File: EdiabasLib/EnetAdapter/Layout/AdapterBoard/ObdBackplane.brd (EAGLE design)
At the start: 32 x 19.5 mm, 10 parts

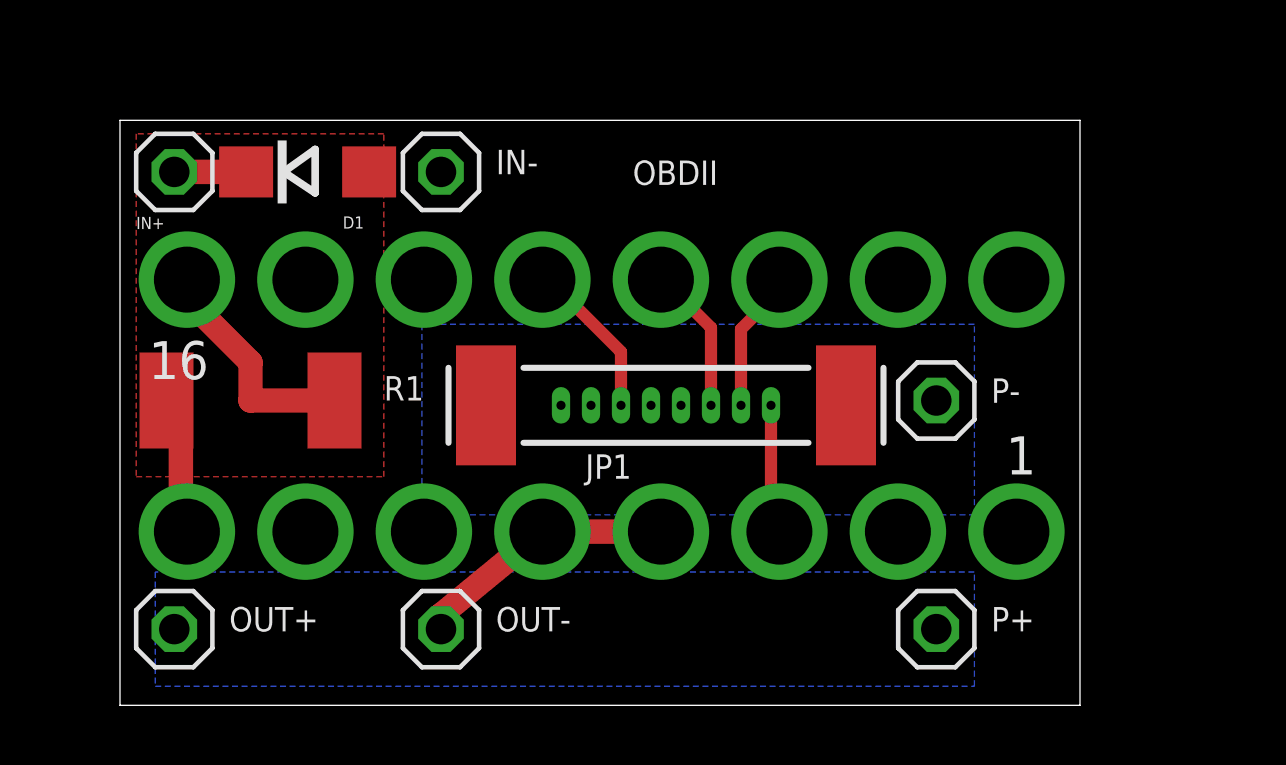
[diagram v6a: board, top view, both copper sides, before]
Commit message: Connector moved
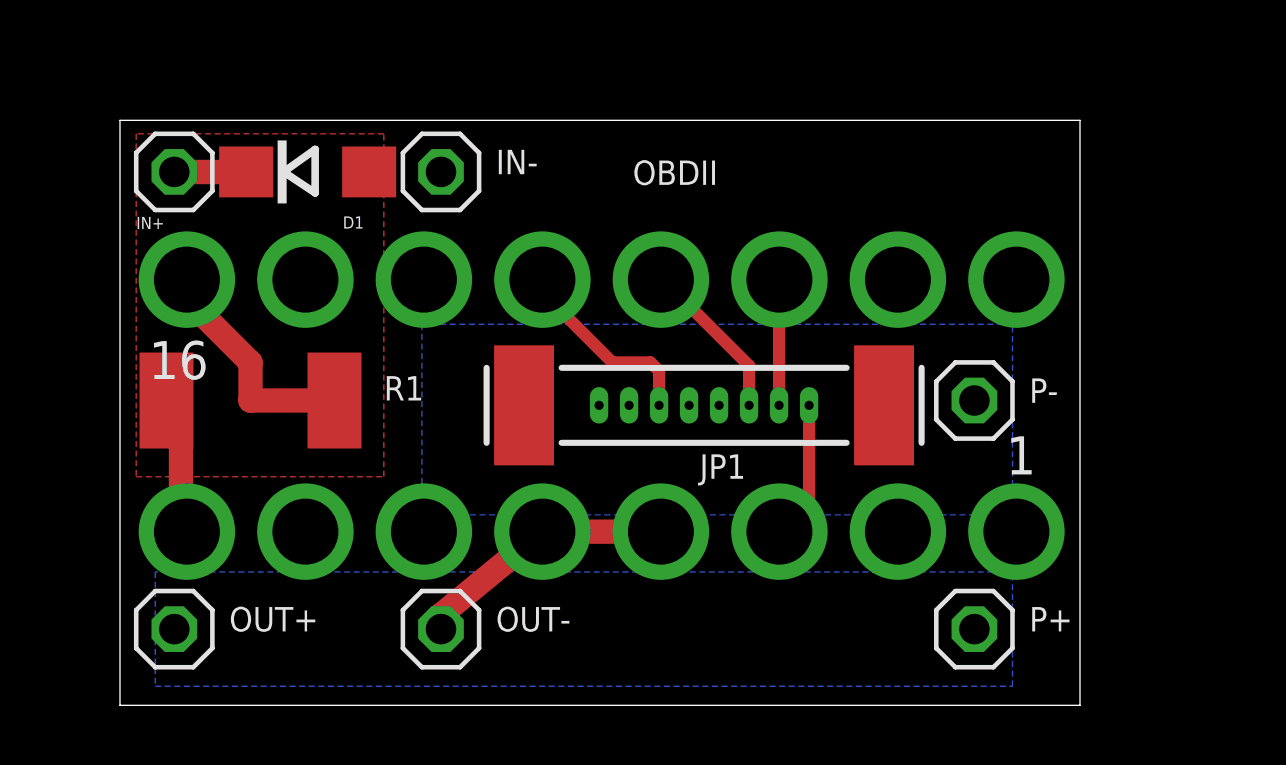
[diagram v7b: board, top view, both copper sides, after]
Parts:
- moved JP1 1.27 mm to (21.5, 10.0)
- moved P+ 1.27 mm to (30.5, 2.54)
- moved P- 1.27 mm to (30.5, 10.2)
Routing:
- net N$6: track 5.40 -> 6.55 mm
- net N$4: track 4.92 -> 5.45 mm
- net N$7: track 4.72 -> 4.19 mm
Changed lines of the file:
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@@
 <attribute name="VALUE" x="10.795" y="8.89" size="0.8128" layer="27"/>
 </element>
-<element name="P+" library="pinhead" package="1X01" value="5V" x="29.21" y="2.54" smashed="yes">
-<attribute name="NAME" x="31.0388" y="2.4638" size="0.8128" layer="25" ratio="10"/>
-<attribute name="VALUE" x="31.115" y="1.27" size="0.8128" layer="27"/>
+<element name="P+" library="pinhead" package="1X01" value="5V" x="30.48" y="2.54" smashed="yes">
+<attribute name="NAME" x="32.3088" y="2.4638" size="0.8128" layer="25" ratio="10"/>
+<attribute name="VALUE" x="32.385" y="1.27" size="0.8128" layer="27"/>
 </element>
-<element name="P-" library="pinhead" package="1X01" value="GND" x="29.21" y="10.16" smashed="yes">
-<attribute name="NAME" x="31.0388" y="10.0838" size="0.8128" layer="25" ratio="10"/>
-<attribute name="VALUE" x="30.48" y="8.89" size="0.8128" layer="27"/>
+<element name="P-" library="pinhead" package="1X01" value="GND" x="30.48" y="10.16" smashed="yes">
+<attribute name="NAME" x="32.3088" y="10.0838" size="0.8128" layer="25" ratio="10"/>
+<attribute name="VALUE" x="31.75" y="8.89" size="0.8128" layer="27"/>
 </element>
-<element name="JP1" library="obd_special" package="1X08M-1MM" value="ETHERNET" x="20.2" y="10" smashed="yes">
-<attribute name="NAME" x="19.05" y="8.365" size="0.8128" layer="25" ratio="14" rot="R180"/>
+<element name="JP1" library="obd_special" package="1X08M-1MM" value="ETHERNET" x="21.47" y="10" smashed="yes">
+<attribute name="NAME" x="22.86" y="8.365" size="0.8128" layer="25" ratio="14" rot="R180"/>
 </element>
 </elements>
@@
 <wire x1="16.08" y1="5.79" x2="20.03" y2="5.79" width="0.8128" layer="1"/>
 <polygon width="0.254" layer="16" spacing="0.254" isolate="0.4064">
-<vertex x="30.48" y="6.35"/>
-<vertex x="30.48" y="12.7"/>
+<vertex x="31.75" y="6.35"/>
+<vertex x="31.75" y="12.7"/>
 <vertex x="12.065" y="12.7"/>
 <vertex x="12.065" y="6.35"/>
@@
 <polygon width="0.254" layer="16" spacing="0.254" isolate="0.4064">
 <vertex x="3.175" y="0.635"/>
-<vertex x="30.48" y="0.635"/>
-<vertex x="30.48" y="4.445"/>
+<vertex x="31.75" y="0.635"/>
+<vertex x="31.75" y="4.445"/>
 <vertex x="3.175" y="4.445"/>
 </polygon>
@@
 <contactref element="OBDII" pad="3"/>
 <contactref element="JP1" pad="8"/>
-<wire x1="23.7" y1="10" x2="23.7" y2="6.07" width="0.4064" layer="1"/>
-<wire x1="23.7" y1="6.07" x2="23.98" y2="5.79" width="0.4064" layer="1"/>
+<wire x1="24.97" y1="10" x2="24.97" y2="6.78" width="0.4064" layer="1"/>
+<wire x1="24.97" y1="6.78" x2="23.98" y2="5.79" width="0.4064" layer="1"/>
 </signal>
 <signal name="N$6">
 <contactref element="OBDII" pad="13"/>
 <contactref element="JP1" pad="3"/>
-<wire x1="18.7" y1="10" x2="18.7" y2="11.78" width="0.4064" layer="1"/>
-<wire x1="18.7" y1="11.78" x2="16.51" y2="13.97" width="0.4064" layer="1"/>
-<wire x1="16.51" y1="13.97" x2="16.3" y2="13.97" width="0.4064" layer="1"/>
-<wire x1="16.3" y1="13.97" x2="16.08" y2="14.19" width="0.4064" layer="1"/>
+<wire x1="19.97" y1="10" x2="19.97" y2="11.145" width="0.4064" layer="1"/>
+<wire x1="19.97" y1="11.145" x2="19.685" y2="11.43" width="0.4064" layer="1"/>
+<wire x1="19.685" y1="11.43" x2="18.415" y2="11.43" width="0.4064" layer="1"/>
+<wire x1="18.415" y1="11.43" x2="16.51" y2="13.335" width="0.4064" layer="1"/>
+<wire x1="16.51" y1="13.335" x2="16.51" y2="13.76" width="0.4064" layer="1"/>
+<wire x1="16.51" y1="13.76" x2="16.08" y2="14.19" width="0.4064" layer="1"/>
 </signal>
 <signal name="N$7">
 <contactref element="OBDII" pad="11"/>
 <contactref element="JP1" pad="7"/>
-<wire x1="22.7" y1="10" x2="22.7" y2="12.54" width="0.4064" layer="1"/>
-<wire x1="22.7" y1="12.54" x2="23.495" y2="13.335" width="0.4064" layer="1"/>
-<wire x1="23.495" y1="13.335" x2="23.495" y2="13.705" width="0.4064" layer="1"/>
-<wire x1="23.495" y1="13.705" x2="23.98" y2="14.19" width="0.4064" layer="1"/>
+<wire x1="23.97" y1="10" x2="23.97" y2="14.18" width="0.4064" layer="1"/>
+<wire x1="23.97" y1="14.18" x2="23.98" y2="14.19" width="0.4064" layer="1"/>
 </signal>
 <signal name="N$4">
 <contactref element="OBDII" pad="12"/>
 <contactref element="JP1" pad="6"/>
-<wire x1="21.7" y1="10" x2="21.7" y2="12.59" width="0.4064" layer="1"/>
-<wire x1="21.7" y1="12.59" x2="20.32" y2="13.97" width="0.4064" layer="1"/>
+<wire x1="22.97" y1="10" x2="22.97" y2="11.32" width="0.4064" layer="1"/>
+<wire x1="22.97" y1="11.32" x2="20.32" y2="13.97" width="0.4064" layer="1"/>
 <wire x1="20.32" y1="13.97" x2="20.25" y2="13.97" width="0.4064" layer="1"/>
 <wire x1="20.25" y1="13.97" x2="20.03" y2="14.19" width="0.4064" layer="1"/>
